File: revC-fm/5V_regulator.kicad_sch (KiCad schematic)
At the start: 18 parts, among them Q10 MMBT4403WT1G, U14 TPS63070

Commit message: working revC
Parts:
- added C34: 10uF, Capacitor_SMD:C_0603_1608Metric, symbol Device:C
- added R58: 10k, Resistor_SMD:R_0603_1608Metric, symbol Device:R_US
- C31: renamed from C42; footprint Capacitor_SMD:C_0805_2012Metric -> Capacitor_SMD:C_1206_3216Metric
- C32: renamed from C43; footprint Capacitor_SMD:C_0805_2012Metric -> Capacitor_SMD:C_1206_3216Metric
- R60: renamed from R91; value 10Meg -> 100k
- renumbered C44 to C33, C46 to C35, C47 to C36, C48 to C37, C45 to C38, Q10 to Q11, R89 to R59, R86 to R61, R90 to R62, R87 to R64, R88 to R65, U14 to U8
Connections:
- net GND: now also C34.2
- net VBUS: now also R58.1; no longer U8.1 (PS/SYNC)
- net Vout: now also C34.1
- new net: R58.2, U8.1 (PS/SYNC)
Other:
- note added: "x3 10uF caps 2 are 0805 1 is 0603 per TI Webench"
- moved on the sheet: C31, C32, C33, C35, C36, C37

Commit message: working revC
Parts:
- removed Q11: MMBT4403WT1G, Package_TO_SOT_SMD:SOT-323_SC-70, symbol mainboard-rescue:Q_PNP_BEC-Device-mainboard-rescue
- removed R61: 1Meg, Resistor_SMD:R_0603_1608Metric, symbol Device:R_US
- removed R64: 10Meg, Resistor_SMD:R_0603_1608Metric, symbol Device:R_US
- added R211 (x2): 0, Resistor_SMD:R_0603_1608Metric, symbol Device:R_US
- added R94: 100k, Resistor_SMD:R_0603_1608Metric, symbol Device:R_US
- C65: renamed from C33; footprint Capacitor_SMD:C_0805_2012Metric -> Capacitor_SMD:C_1206_3216Metric
- L5: renamed from L2; footprint mainboard-SLI:L_Bourns_SRN8040TA -> SierraLobo:L_Bourns_SRN8040TA
- R95: renamed from R58; value 10k -> 100k
- U18: renamed from U8; footprint mainboard-SLI:TPS63070RNMR -> SierraLobo:TPS63070RNMR; symbol mainboard_SLI:TPS63070 -> SierraLobo:TPS63070
- renumbered C34 to C59, C35 to C60, C36 to C61, C37 to C62, C31 to C63, C32 to C64, C38 to C66, R65 to R100, R59 to R101, R62 to R102, R60 to R99, TH1 to TH2
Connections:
- net EN: now also R23.2, R94.2; no longer R23.1, U18.14 (EN)
- net VBUS: now also R94.1
- net Vout: now also R211.1; no longer R101.1
- net PG: now reaches R99.2, U18.2 (PG)
- new net: R23.1, U18.14 (EN)
- new net: R101.1, R211.1, R211.2
- new net SEN: R211.2
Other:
- note added: "5V 2A MAX"
- note added: "double check ti wb design"
- note removed: "5V 2A MAX large amt of headroom here"
- note removed: "active low in this case"
- note removed: "x3 10uF caps 2 are 0805 1 is 0603 per TI Webench"
- moved on the sheet: C59, C60, C61, C62, C63, C64, C65, R100, R101, R102, R23, R99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

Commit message: routing fm
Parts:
- removed R100: 10k, Resistor_SMD:R_0603_1608Metric, symbol Device:R_US
- removed R211 (x2): 0, Resistor_SMD:R_0603_1608Metric, symbol Device:R_US
- removed R23: 1k, Resistor_SMD:R_0603_1608Metric, symbol Device:R_US
- removed TH2: 10k, Resistor_SMD:R_0603_1608Metric, symbol Device:Thermistor_NTC_US
- added D17: YEL, LED_SMD:LED_0603_1608Metric, symbol Device:LED
- added Q34: MMDT3946, Package_TO_SOT_SMD:SOT-363_SC-70-6, symbol Transistor_BJT:MMDT3946
- added R108: 1k, Resistor_SMD:R_0603_1608Metric, symbol Device:R_US
- added R36: 100k, Resistor_SMD:R_0603_1608Metric, symbol Device:R_US
- added R92: 10k, Resistor_SMD:R_0603_1608Metric, symbol Device:R_US
- added R92: 2.7k, Resistor_SMD:R_0603_1608Metric, symbol Device:R_US
- C65: footprint Capacitor_SMD:C_1206_3216Metric -> Capacitor_SMD:C_0603_1608Metric
- R94, R95, R99: value 100k -> 1Meg
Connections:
- net EN: now also R94.1, R36.1; no longer R94.2
- net GND: now also R94.2, Q34.1 (E1), Q34.3 (C2), R108.2; no longer U18.15 (VSEL), U18.6 (FB2)
- net PG: now also Q34.5 (B2)
- net at U18.14 (EN): now also R36.2
- net VOUT: now reaches R101.1
- net VOUT: now also C59.1, C60.1, C61.1, C62.1, U18.7 (VOUT)
- net VBUS renamed VIN
- net VIN: no longer R94.1
- removed net Vout: C59.1, C60.1, C61.1, C62.1, R99.1, U18.7 (VOUT)
- new net: R108.1, U18.15 (VSEL)
- new net: D17.1 (K), Q34.6 (C1)
- new net: D17.2 (A), R92.1
- new net: Q34.2 (B1), Q34.4 (E2), R92.1
- new net LED_PWR: R92.2, R92.2
- new net VIO: R99.1
- no-connect marks 0 -> 1
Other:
- added sheet Temp Sensor 2 (temp_senkicad_sch.kicad_sch)
- note added: "Keeps regulator off by default."
- note added: "Place close to IC"
- note removed: "could possibly adjust inductor / caps in future to boost low current eff if power req. decreases"
- note removed: "double check ti wb design"
- moved on the sheet: C60, C61, C62, C63, C64, C65, C66, R101, R102

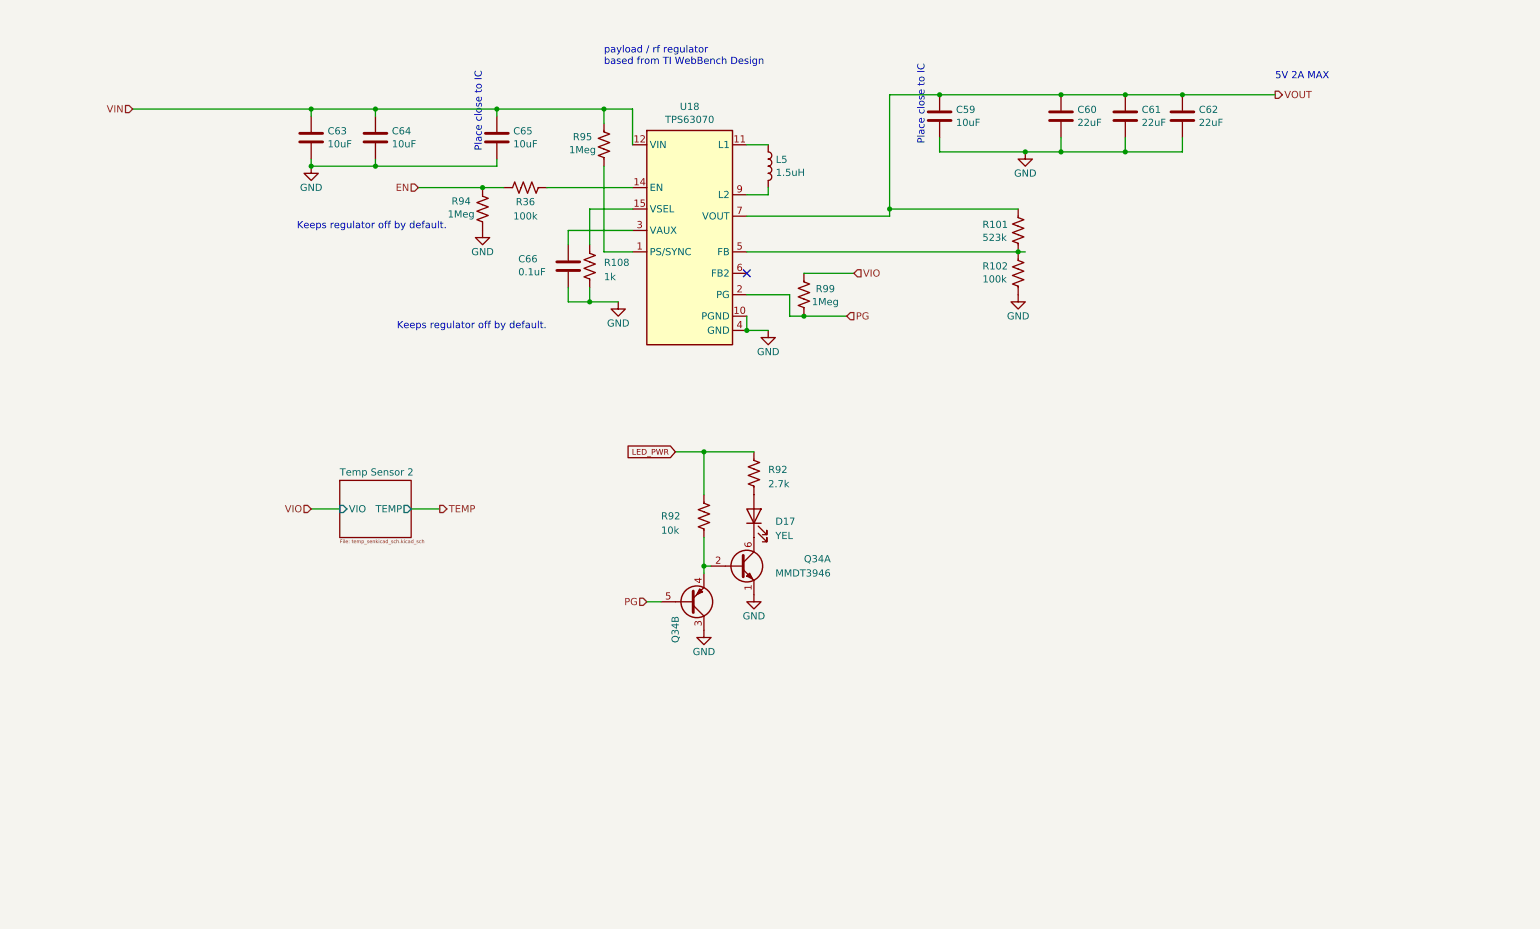
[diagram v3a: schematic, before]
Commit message: updated analog , solar comp, layout
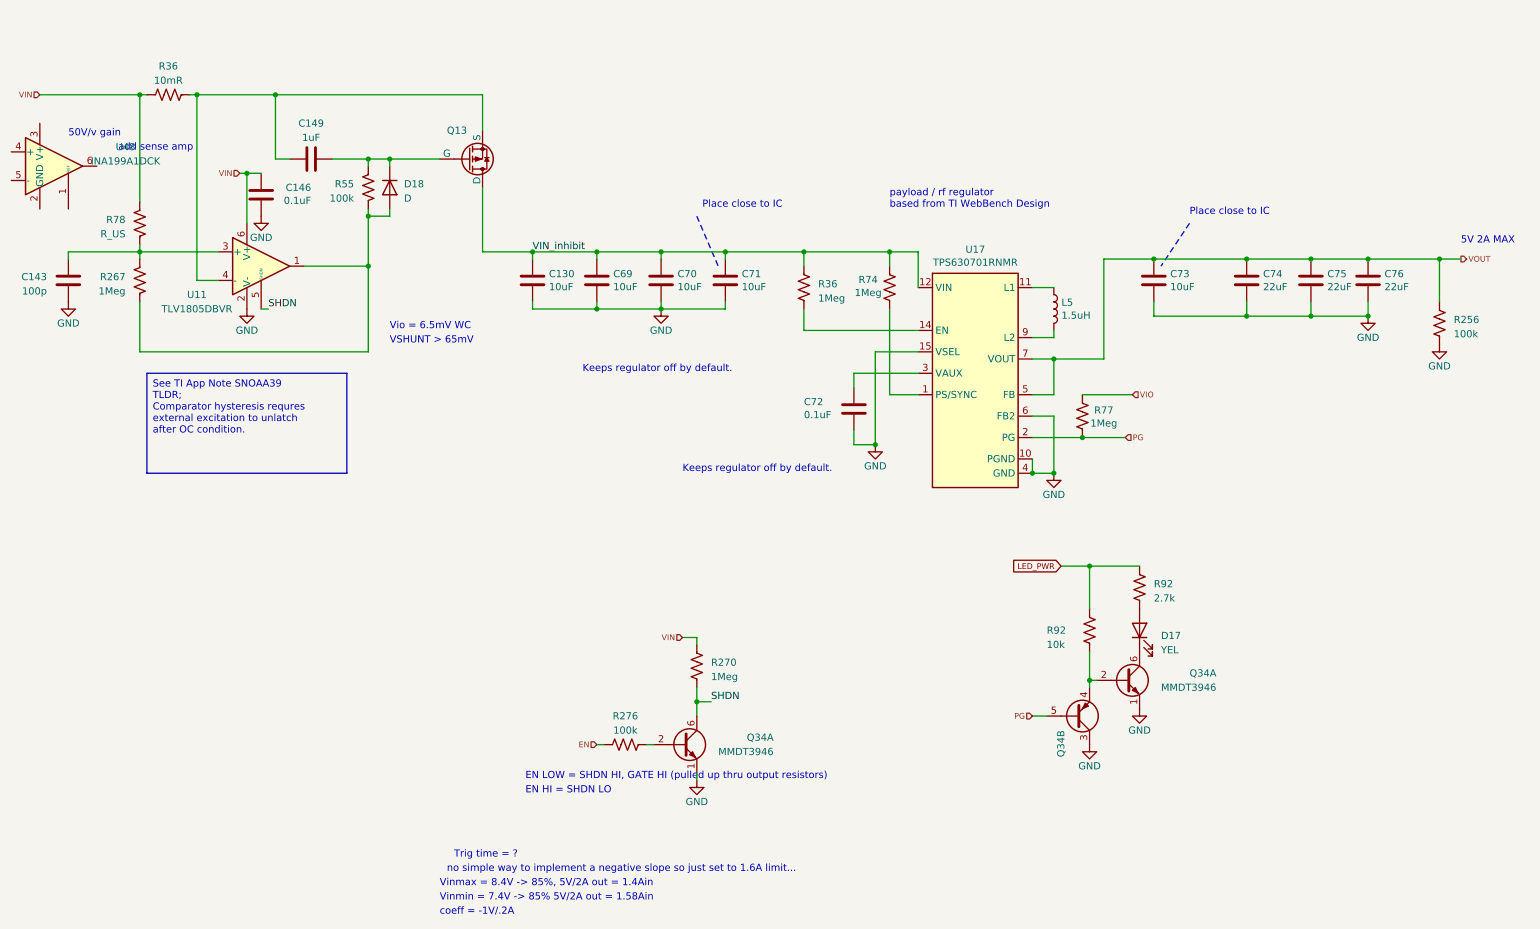
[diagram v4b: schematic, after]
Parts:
- removed R101: 523k, Resistor_SMD:R_0603_1608Metric, symbol Device:R_US
- removed R102: 100k, Resistor_SMD:R_0603_1608Metric, symbol Device:R_US
- removed R108: 1k, Resistor_SMD:R_0603_1608Metric, symbol Device:R_US
- removed R94: 1Meg, Resistor_SMD:R_0603_1608Metric, symbol Device:R_US
- added C130: 10uF, Capacitor_SMD:C_0805_2012Metric, symbol Device:C
- added C143: 100p, Capacitor_SMD:C_0402_1005Metric, symbol Device:C
- added C146: 0.1uF, Capacitor_SMD:C_0402_1005Metric, symbol Device:C
- added C149: 1uF, Capacitor_SMD:C_0402_1005Metric, symbol Device:C
- added D18: D, symbol Device:D
- added Q13: BSZ180P03NS3GATMA1, SierraLobo:PG-TSDSON-8_3.3x3.3mm, symbol SierraLobo:BSZ086
- added Q34: MMDT3946, Package_TO_SOT_SMD:SOT-363_SC-70-6, symbol Transistor_BJT:MMDT3946
- added R256, R55: 100k, Resistor_SMD:R_0603_1608Metric, symbol Device:R_US
- added R267, R270: 1Meg, symbol Device:R_US
- added R276: 100k, symbol Device:R_US
- added R36: 10mR, Resistor_SMD:R_0805_2012Metric, symbol Device:R_US
- added R78: R_US, symbol Device:R_US
- added U11: TLV1805DBVR, Package_TO_SOT_SMD:SOT-23-6, symbol SierraLobo:TLV1805DBVR
- added U48: INA199A1DCK, Package_TO_SOT_SMD:SOT-363_SC-70-6, symbol Amplifier_Current:INA199xxDCK
- C69: renamed from C63; footprint Capacitor_SMD:C_1206_3216Metric -> Capacitor_SMD:C_0805_2012Metric
- C70: renamed from C64; footprint Capacitor_SMD:C_1206_3216Metric -> Capacitor_SMD:C_0805_2012Metric
- C72: renamed from C66; footprint Capacitor_SMD:C_0603_1608Metric -> Capacitor_SMD:C_0402_1005Metric
- L5: footprint SierraLobo:L_Bourns_SRN8040TA -> Inductor_SMD:L_Wuerth_HCI-5040
- R36: value 100k -> 1Meg
- U17: renamed from U18; value TPS63070 -> TPS630701RNMR
- renumbered C65 to C71, C59 to C73, C60 to C74, C61 to C75, C62 to C76, R95 to R74, R99 to R77
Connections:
- net EN: now also R276.1; no longer R36.1
- net GND: now also U17.15 (VSEL), U17.6 (FB2), C130.2, C143.2, C146.1, Q34.1 (E1), R256.2, U11.2 (V-)
- net VIN: now also C146.2, R270.1, R36.1, R78.1, U11.6 (V+); no longer C69.1, C70.1, C71.1, R74.1, U17.12 (VIN)
- net VOUT: now also U17.5 (FB), R256.1
- net at U17.14 (EN): now also R36.1; no longer R36.2
- new net: C149.2, D18.1 (K), Q13.4 (G), R55.1
- new net: D18.2 (A), R267.2, R55.2, U11.1
- new net: Q34.2 (B1), R276.2
- new net: C149.1, Q13.1 (S), R36.2, U11.4 (-)
- new net: C143.1, R267.1, R78.2, U11.3 (+)
- new net SHDN: Q34.6 (C1), R270.2, U11.5 (SHDN)
- new net VIN_inhibit: C130.1, C69.1, C70.1, C71.1, Q13.5 (D), R36.2, R74.1, U17.12 (VIN)
- no-connect marks 1 -> 0
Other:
- removed sheet Temp Sensor 2
- note added: "50V/v gain"
- note added: "EN HI = SHDN LO"
- note added: "EN LOW = SHDN HI, GATE HI (pulled up thru output resistors)"
- note added: "Trig time = ?"
- note added: "VSHUNT > 65mV"
- note added: "Vinmax = 8.4V -> 85%, 5V/2A out = 1.4Ain"
- note added: "Vinmin = 7.4V -> 85% 5V/2A out = 1.58Ain"
- note added: "Vio = 6.5mV WC"
- note added: "add sense amp"
- note added: "coeff = -1V/.2A"
- note added: "no simple way to implement a negative slope so just set to 1.6A limit..."
- moved on the sheet: C69, C70, C71, C72, C73, C74, C75, C76, D17, L5, Q34A, Q34B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

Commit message: routing
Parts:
- removed C143: 100p, Capacitor_SMD:C_0402_1005Metric, symbol Device:C
- removed C146: 0.1uF, Capacitor_SMD:C_0402_1005Metric, symbol Device:C
- removed C149: 1uF, Capacitor_SMD:C_0402_1005Metric, symbol Device:C
- removed D18: D, symbol Device:D
- removed Q13: BSZ180P03NS3GATMA1, SierraLobo:PG-TSDSON-8_3.3x3.3mm, symbol SierraLobo:BSZ086
- removed Q34: MMDT3946, Package_TO_SOT_SMD:SOT-363_SC-70-6, symbol Transistor_BJT:MMDT3946
- removed R267, R270: 1Meg, symbol Device:R_US
- removed R276: 100k, symbol Device:R_US
- removed R36: 10mR, Resistor_SMD:R_0805_2012Metric, symbol Device:R_US
- removed R36: 1Meg, Resistor_SMD:R_0603_1608Metric, symbol Device:R_US
- removed R55: 100k, Resistor_SMD:R_0603_1608Metric, symbol Device:R_US
- removed R78: R_US, symbol Device:R_US
- removed U11: TLV1805DBVR, Package_TO_SOT_SMD:SOT-23-6, symbol SierraLobo:TLV1805DBVR
- removed U48: INA199A1DCK, Package_TO_SOT_SMD:SOT-363_SC-70-6, symbol Amplifier_Current:INA199xxDCK
- added R66: 1Meg, Resistor_SMD:R_0603_1608Metric, symbol Device:R_US
- C80: renamed from C72; footprint Capacitor_SMD:C_0402_1005Metric -> Capacitor_SMD:C_0603_1608Metric
- renumbered C130 to C72, C69 to C73, C70 to C74, C71 to C75, C73 to C76, C74 to C77, C75 to C78, C76 to C79, R74 to R67, R77 to R69, U17 to U19
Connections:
- net at U19.14 (EN): now also R66.2
- net VIN_inhibit renamed OCP/VOUT
- net OCP/VOUT: now also R66.1
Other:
- added sheet OCP (ocp_detector.kicad_sch)
- note added: "Heirarchal Pin Descriptions: EN = enables PFET before regulator ~{ALERT} = OCP alert, turns off PFET, toggle LATCH to clear LATCH = assign normally high, pull low to clear alert LIMIT = OCP trip setting resistor."
- note removed: "50V/v gain"
- note removed: "EN HI = SHDN LO"
- note removed: "EN LOW = SHDN HI, GATE HI (pulled up thru output resistors)"
- note removed: "Keeps regulator off by default."
- note removed: "Trig time = ?"
- note removed: "VSHUNT > 65mV"
- note removed: "Vinmax = 8.4V -> 85%, 5V/2A out = 1.4Ain"
- note removed: "Vinmin = 7.4V -> 85% 5V/2A out = 1.58Ain"
- note removed: "Vio = 6.5mV WC"
- note removed: "add sense amp"
- note removed: "coeff = -1V/.2A"
- note removed: "no simple way to implement a negative slope so just set to 1.6A limit..."
- moved on the sheet: C72, C73, C74, C75, C76, C77, C78, C79, C80, D17, L5, Q34A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

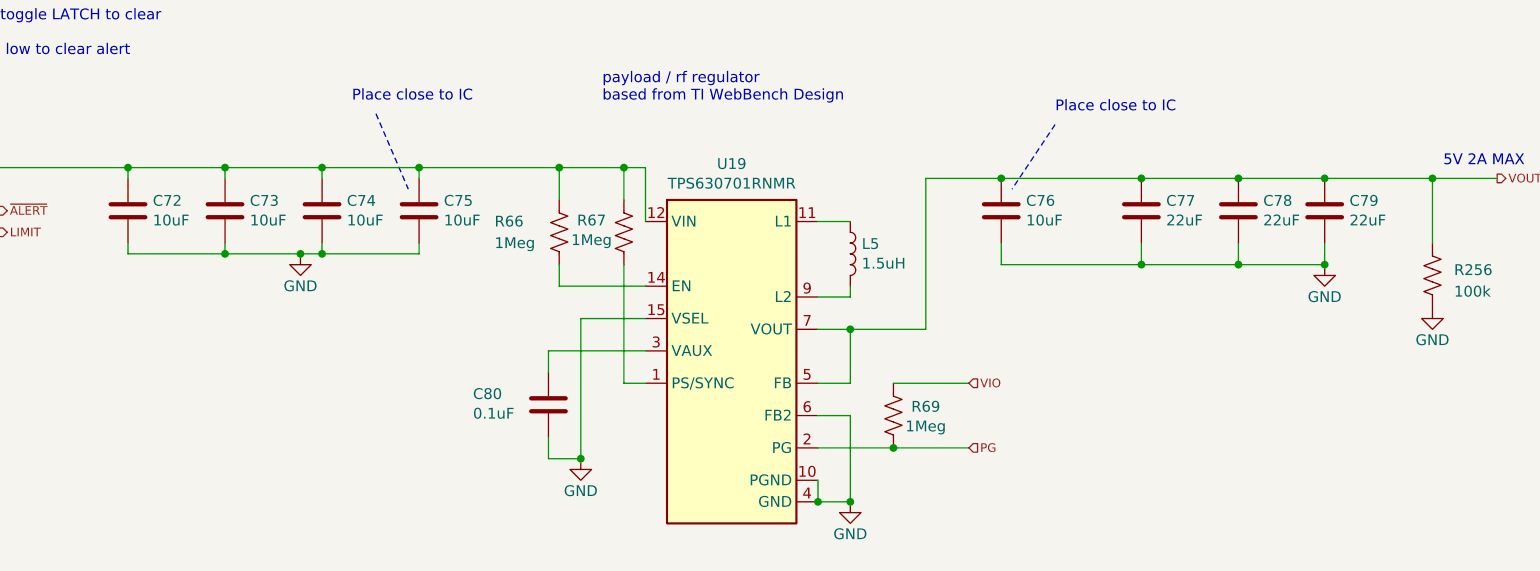
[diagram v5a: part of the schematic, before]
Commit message: changed RF connector to TH
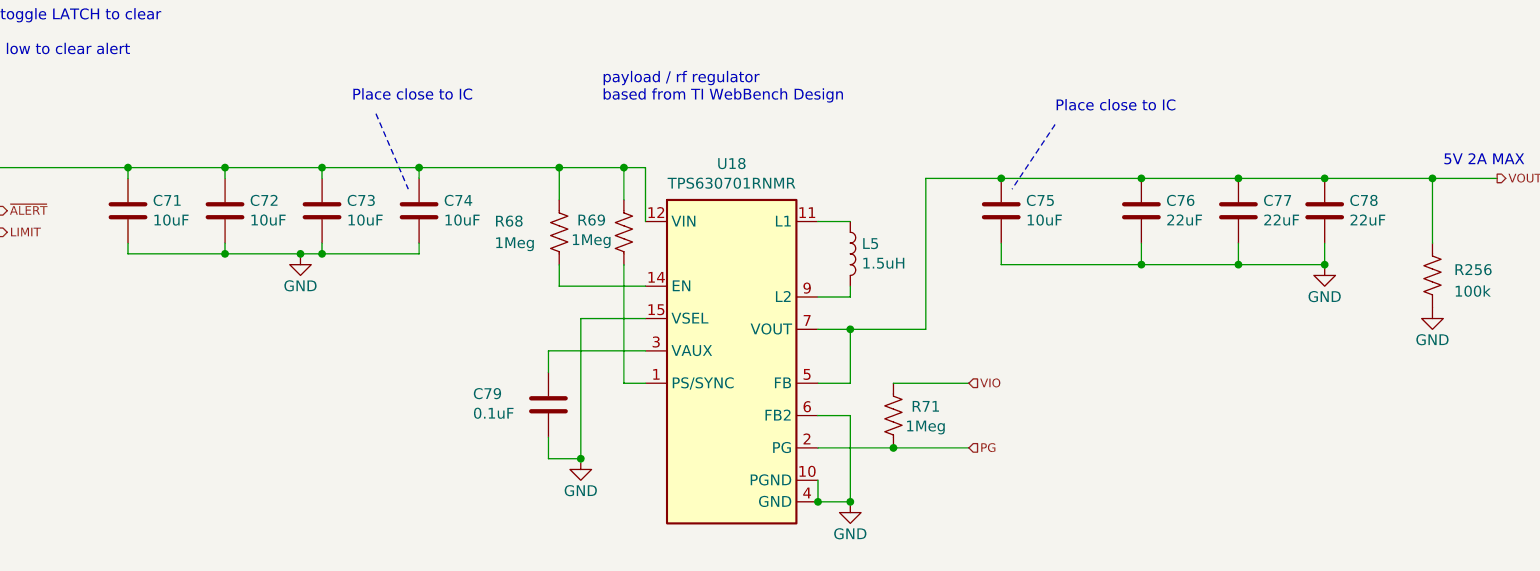
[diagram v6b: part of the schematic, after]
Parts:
- L5: footprint Inductor_SMD:L_Wuerth_HCI-5040 -> SierraLobo:L_Wuerth_HCI-5040
- renumbered C72 to C71, C73 to C72, C74 to C73, C75 to C74, C76 to C75, C77 to C76, C78 to C77, C79 to C78, C80 to C79, R66 to R68, R67 to R69, R69 to R71, U19 to U18

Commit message: working revC review changes
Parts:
- renumbered C71 to C72, C72 to C73, C73 to C74, C74 to C75, C75 to C76, C76 to C77, C77 to C78, C78 to C79, C79 to C80, R68 to R74, R69 to R75, R71 to R77, U18 to U19

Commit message: working revC
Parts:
- removed D17: YEL, LED_SMD:LED_0603_1608Metric, symbol Device:LED
- removed Q34: MMDT3946, Package_TO_SOT_SMD:SOT-363_SC-70-6, symbol Transistor_BJT:MMDT3946
- removed R92: 10k, Resistor_SMD:R_0603_1608Metric, symbol Device:R_US
- removed R92: 2.7k, Resistor_SMD:R_0603_1608Metric, symbol Device:R_US
- added R267: 0, Resistor_SMD:R_0603_1608Metric, symbol Device:R_US
- added R270: DNP, Resistor_SMD:R_0603_1608Metric, symbol Device:R_US
- C60: renamed from C72; Mfr. Part No (none) -> CGA4J1X7S1E106K125AE
- C61: renamed from C73; Mfr. Part No (none) -> CGA4J1X7S1E106K125AE
- C62: renamed from C74; Mfr. Part No (none) -> CGA4J1X7S1E106K125AE
- C63: renamed from C75; Mfr. Part No (none) -> GRT188R61E106ME13D
- C64: renamed from C76; Mfr. Part No (none) -> GRT188R61E106ME13D
- C65: renamed from C77; Mfr. Part No (none) -> GRT21BR61C226ME13K
- C66: renamed from C78; Mfr. Part No (none) -> GRT21BR61C226ME13K
- C67: renamed from C79; Mfr. Part No (none) -> GRT21BR61C226ME13K
- C68: renamed from C80; footprint Capacitor_SMD:C_0603_1608Metric -> Capacitor_SMD:C_0402_1005Metric
- L4: renamed from L5; Mfr. Part No (none) -> 744316150
- R256: footprint Resistor_SMD:R_0603_1608Metric -> Resistor_SMD:R_0402_1005Metric
- R58: renamed from R74; footprint Resistor_SMD:R_0603_1608Metric -> Resistor_SMD:R_0402_1005Metric
- R59: renamed from R75; footprint Resistor_SMD:R_0603_1608Metric -> Resistor_SMD:R_0402_1005Metric
- R61: renamed from R77; footprint Resistor_SMD:R_0603_1608Metric -> Resistor_SMD:R_0402_1005Metric
- U18: renamed from U19; Mfr. Part No (none) -> TPS630701RNMR
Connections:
- net GND: now also R270.2
- net VOUT: now also R267.1; no longer U18.5 (FB)
- net OCP/VOUT renamed VBUS_IN
- new net: R267.2, R270.1, U18.5 (FB)
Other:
- moved on the sheet: R256
